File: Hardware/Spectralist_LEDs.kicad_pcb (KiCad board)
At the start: 2 copper layers, 26 parts, among them U1 PCA9956B_LED_Driver

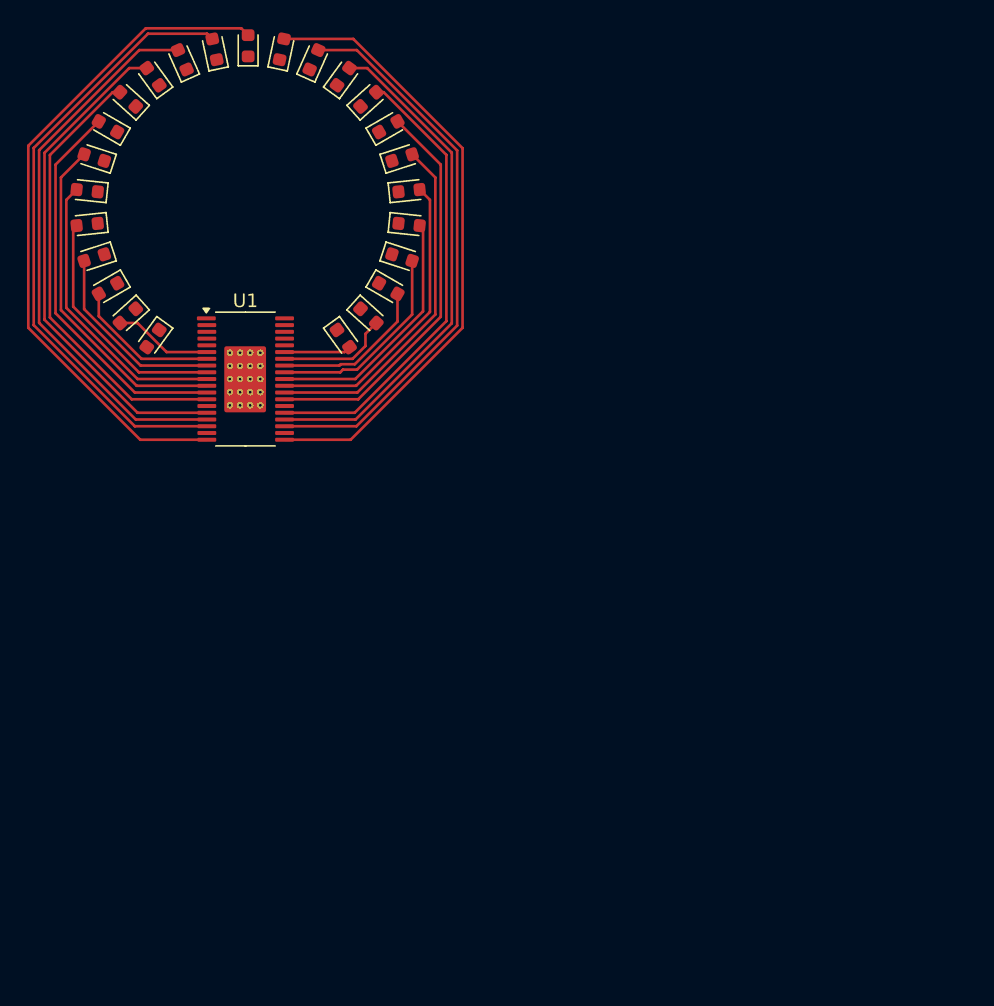
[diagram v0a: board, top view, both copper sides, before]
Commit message: Schematic updates
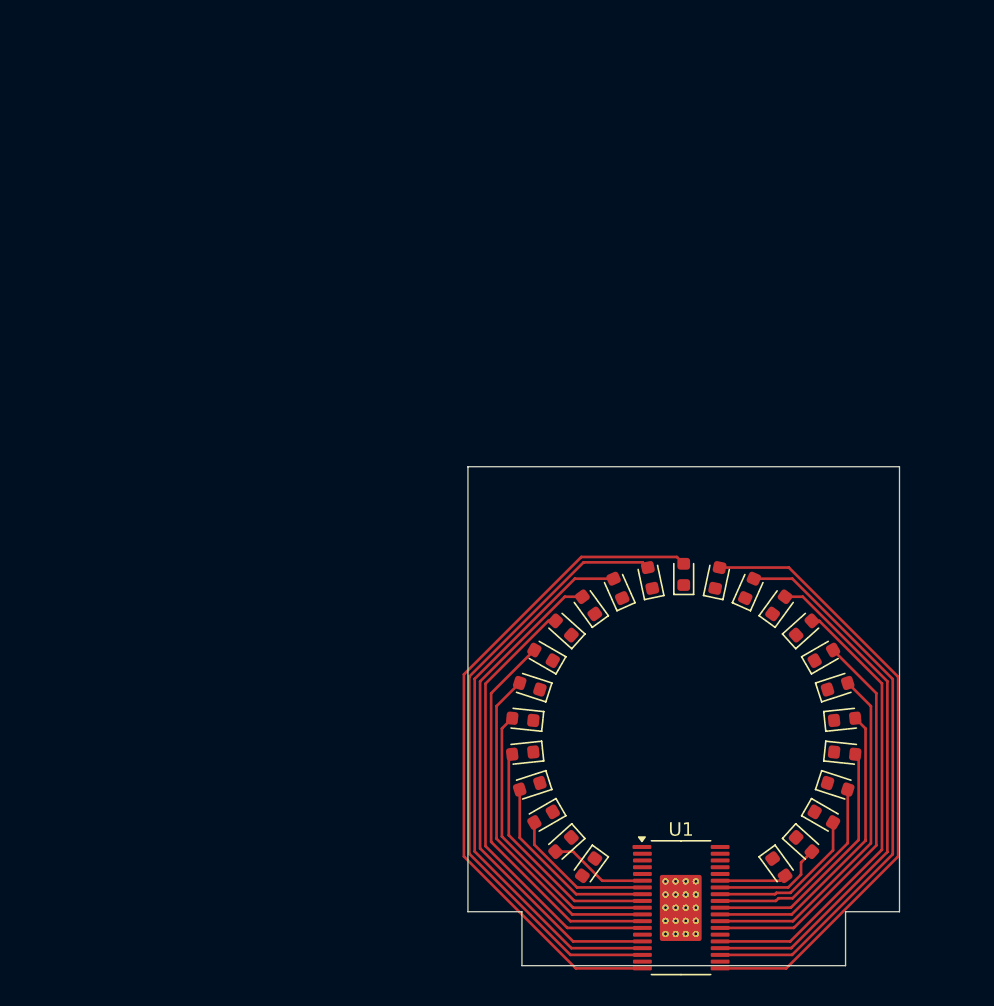
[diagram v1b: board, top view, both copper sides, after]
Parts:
- moved D13 50.8 mm to (132.5, 90.2)
- moved D14 50.8 mm to (134.9, 91.0)
- moved D15 50.8 mm to (137.1, 92.3)
- moved D2 50.8 mm to (119.6, 108.0)
- moved D7 50.8 mm to (119.6, 96.0)
- moved U1 50.8 mm to (129.8, 114.7)
- moved D1 50.8 mm to (121.1, 110.0)
- moved D11 50.8 mm to (127.5, 90.2)
- moved D18 50.8 mm to (141.4, 98.3)
- moved D22 50.8 mm to (140.4, 108.0)
- moved D24 50.8 mm to (137.1, 111.7)
- moved D5 50.8 mm to (118.1, 100.7)
- moved D6 50.8 mm to (118.6, 98.3)
- moved D8 50.8 mm to (121.1, 94.0)
- moved D9 50.8 mm to (122.9, 92.3)
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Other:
- board outline added: 32 x 37 mm

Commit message: Updates to LED board
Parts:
- added C1: 100nF, Capacitor_SMD:C_0603_1608Metric, F.Cu at (135.7, 105.0)
- added C2: 10uF, Capacitor_SMD:C_0805_2012Metric, F.Cu at (112.4, 105.2)
- added J1: Conn_01x03_Pin, Connector_PinHeader_2.54mm:PinHeader_1x03_P2.54mm_Vertical, F.Cu at (132.5, 84.5)
- added J2: Conn_01x02_Pin, Connector_PinHeader_2.54mm:PinHeader_1x02_P2.54mm_Vertical, F.Cu at (112.4, 110.1)
- added J3: Conn_01x02_Pin, Connector_PinHeader_2.54mm:PinHeader_1x02_P2.54mm_Vertical, F.Cu at (147.8, 110.0)
- added R1: 10k, Resistor_SMD:R_0603_1608Metric, F.Cu at (122.4, 105.1)
- added R2: 2k, Resistor_SMD:R_0603_1608Metric, F.Cu at (124.3, 105.1)
- added R3: 10k, Resistor_SMD:R_0603_1608Metric, F.Cu at (138.0, 105.0)
- moved U1 2.61 mm to (129.8, 112.1)
- turned D1 to 42 degrees
- turned D10 to -66 degrees
- turned D11 to -78 degrees
- turned D12 to -90 degrees
- turned D13 to -102 degrees
- turned D14 to -114 degrees
- turned D15 to -126 degrees
- turned D16 to -138 degrees
- turned D17 to -150 degrees
- turned D18 to -162 degrees
- turned D19 to -174 degrees
- turned D2 to 30 degrees
- turned D20 to 174 degrees
- turned D21 to 162 degrees
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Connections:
- D1 pad 1: GND -> Net-(D1-K)
- D1 pad 2: Net-(D1-A) -> +12V
- D10 pad 1: GND -> Net-(D10-K)
- D10 pad 2: Net-(D10-A) -> +12V
- D11 pad 1: GND -> Net-(D11-K)
- D11 pad 2: Net-(D11-A) -> +12V
- D12 pad 1: GND -> Net-(D12-K)
- D12 pad 2: Net-(D12-A) -> +12V
- D13 pad 1: GND -> Net-(D13-K)
- D13 pad 2: Net-(D13-A) -> +12V
- D14 pad 1: GND -> Net-(D14-K)
- D14 pad 2: Net-(D14-A) -> +12V
- D15 pad 1: GND -> Net-(D15-K)
- D15 pad 2: Net-(D15-A) -> +12V
- D16 pad 1: GND -> Net-(D16-K)
- D16 pad 2: Net-(D16-A) -> +12V
- D17 pad 1: GND -> Net-(D17-K)
- D17 pad 2: Net-(D17-A) -> +12V
- D18 pad 1: GND -> Net-(D18-K)
- D18 pad 2: Net-(D18-A) -> +12V
- D19 pad 1: GND -> Net-(D19-K)
- D19 pad 2: Net-(D19-A) -> +12V
- D2 pad 1: GND -> Net-(D2-K)
- D2 pad 2: Net-(D2-A) -> +12V
- D20 pad 1: GND -> Net-(D20-K)
- D20 pad 2: Net-(D20-A) -> +12V
- D21 pad 1: GND -> Net-(D21-K)
- D21 pad 2: Net-(D21-A) -> +12V
- D22 pad 1: GND -> Net-(D22-K)
- D22 pad 2: Net-(D22-A) -> +12V
- D23 pad 1: GND -> Net-(D23-K)
- D23 pad 2: Net-(D23-A) -> +12V
- D24 pad 1: GND -> Net-(D24-K)
- D24 pad 2: Net-(D24-A) -> +12V
- D25 pad 2: unconnected-(D25-A-Pad2) -> Net-(D25-A)
- D3 pad 1: GND -> Net-(D3-K)
- D3 pad 2: Net-(D3-A) -> +12V
- D4 pad 1: GND -> Net-(D4-K)
- D4 pad 2: Net-(D4-A) -> +12V
- D5 pad 1: GND -> Net-(D5-K)
- D5 pad 2: Net-(D5-A) -> +12V
- D6 pad 1: GND -> Net-(D6-K)
- D6 pad 2: Net-(D6-A) -> +12V
- D7 pad 1: GND -> Net-(D7-K)
- D7 pad 2: Net-(D7-A) -> +12V
- D8 pad 1: GND -> Net-(D8-K)
- D8 pad 2: Net-(D8-A) -> +12V
- D9 pad 1: GND -> Net-(D9-K)
- D9 pad 2: Net-(D9-A) -> +12V
- U1 pad 1: unconnected-(U1-REXT-Pad1) -> Net-(U1-REXT)
- U1 pad 10: Net-(D5-A) -> Net-(D5-K)
- U1 pad 11: Net-(D6-A) -> Net-(D6-K)
- U1 pad 12: Net-(D7-A) -> Net-(D7-K)
- U1 pad 13: Net-(D8-A) -> Net-(D8-K)
- U1 pad 15: Net-(D9-A) -> Net-(D9-K)
- U1 pad 16: Net-(D10-A) -> Net-(D10-K)
- U1 pad 17: Net-(D11-A) -> Net-(D11-K)
- U1 pad 19: Net-(D12-A) -> Net-(D12-K)
- U1 pad 20: Net-(D13-A) -> Net-(D13-K)
- U1 pad 22: Net-(D14-A) -> Net-(D14-K)
- U1 pad 23: Net-(D15-A) -> Net-(D15-K)
- U1 pad 24: Net-(D16-A) -> Net-(D16-K)
- U1 pad 26: Net-(D17-A) -> Net-(D17-K)
- U1 pad 27: Net-(D18-A) -> Net-(D18-K)
- U1 pad 28: Net-(D19-A) -> Net-(D19-K)
- U1 pad 29: Net-(D20-A) -> Net-(D20-K)
- U1 pad 30: Net-(D21-A) -> Net-(D21-K)
- U1 pad 31: Net-(D22-A) -> Net-(D22-K)
- U1 pad 32: Net-(D23-A) -> Net-(D23-K)
- U1 pad 33: Net-(D24-A) -> Net-(D24-K)
- U1 pad 35: unconnected-(U1-~{RESET}-Pad35) -> Net-(U1-~{RESET})
- U1 pad 36: unconnected-(U1-SCL-Pad36) -> /LED_SCL
- U1 pad 37: unconnected-(U1-SDA-Pad37) -> /LED_SDA
- U1 pad 38: unconnected-(U1-VDD-Pad38) -> +3.3V
- U1 pad 6: Net-(D1-A) -> Net-(D1-K)
- U1 pad 7: Net-(D2-A) -> Net-(D2-K)
- U1 pad 8: Net-(D3-A) -> Net-(D3-K)
- U1 pad 9: Net-(D4-A) -> Net-(D4-K)
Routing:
- net +12V: track 0.00 -> 73.2 mm, vias 0 -> 1
- net Net-(D12-A): track 50.3 -> 0.00 mm
- net GND: track 0.00 -> 48.4 mm, vias 0 -> 12
- net Net-(D13-A): track 46.6 -> 0.00 mm
- net Net-(D11-A): track 46.0 -> 0.00 mm
- net Net-(D14-A): track 42.3 -> 0.00 mm
- net Net-(D10-A): track 41.6 -> 0.00 mm
- net Net-(D15-K): track 0.00 -> 38.2 mm
- net Net-(D15-A): track 38.2 -> 0.00 mm
- net Net-(D9-K): track 0.00 -> 37.7 mm
- net Net-(D9-A): track 37.5 -> 0.00 mm
- net Net-(D11-K): track 0.00 -> 35.3 mm, vias 0 -> 2
- net Net-(D16-A): track 34.3 -> 0.00 mm
- net Net-(D16-K): track 0.00 -> 34.2 mm
- net Net-(D8-K): track 0.00 -> 33.9 mm
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- added copper zone on B.Cu, net GND
- added copper zone on F.Cu, net GND
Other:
- board size 32 x 37 mm -> 40 x 37 mm

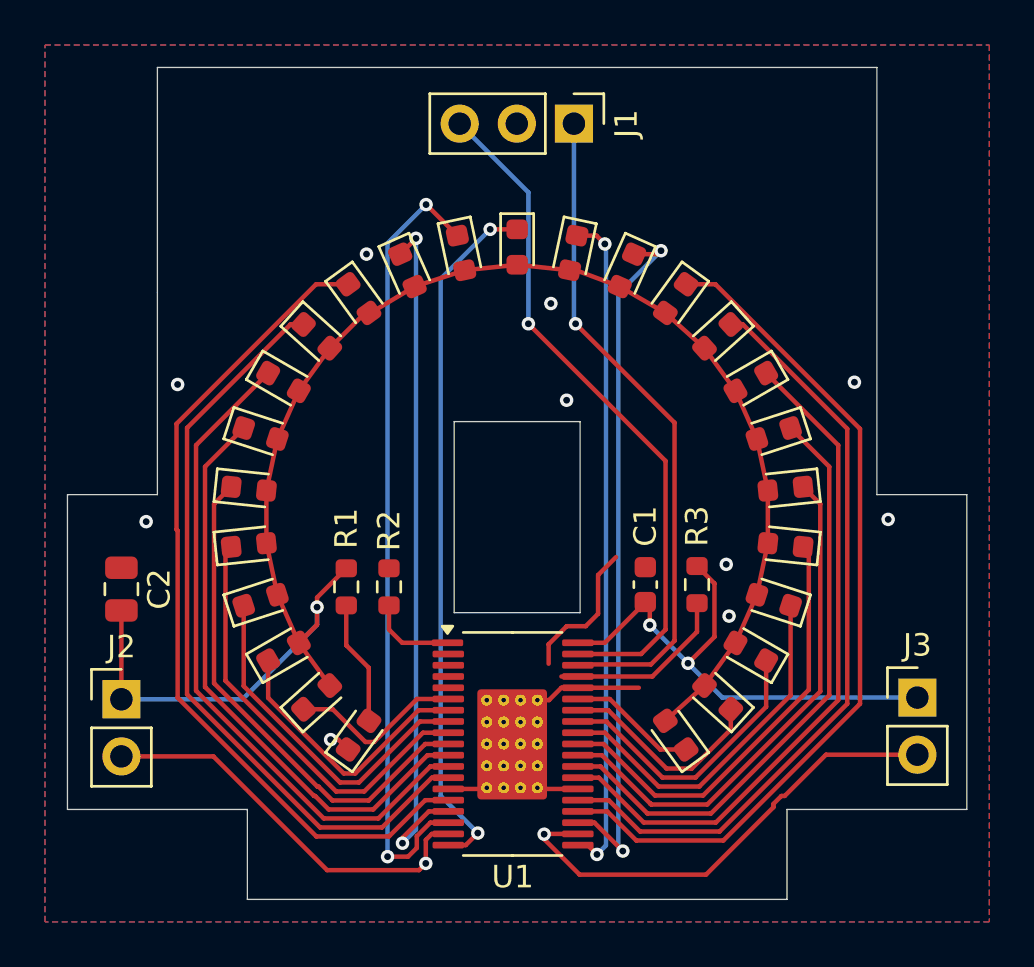
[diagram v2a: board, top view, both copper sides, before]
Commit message: Curvy traces on LED board
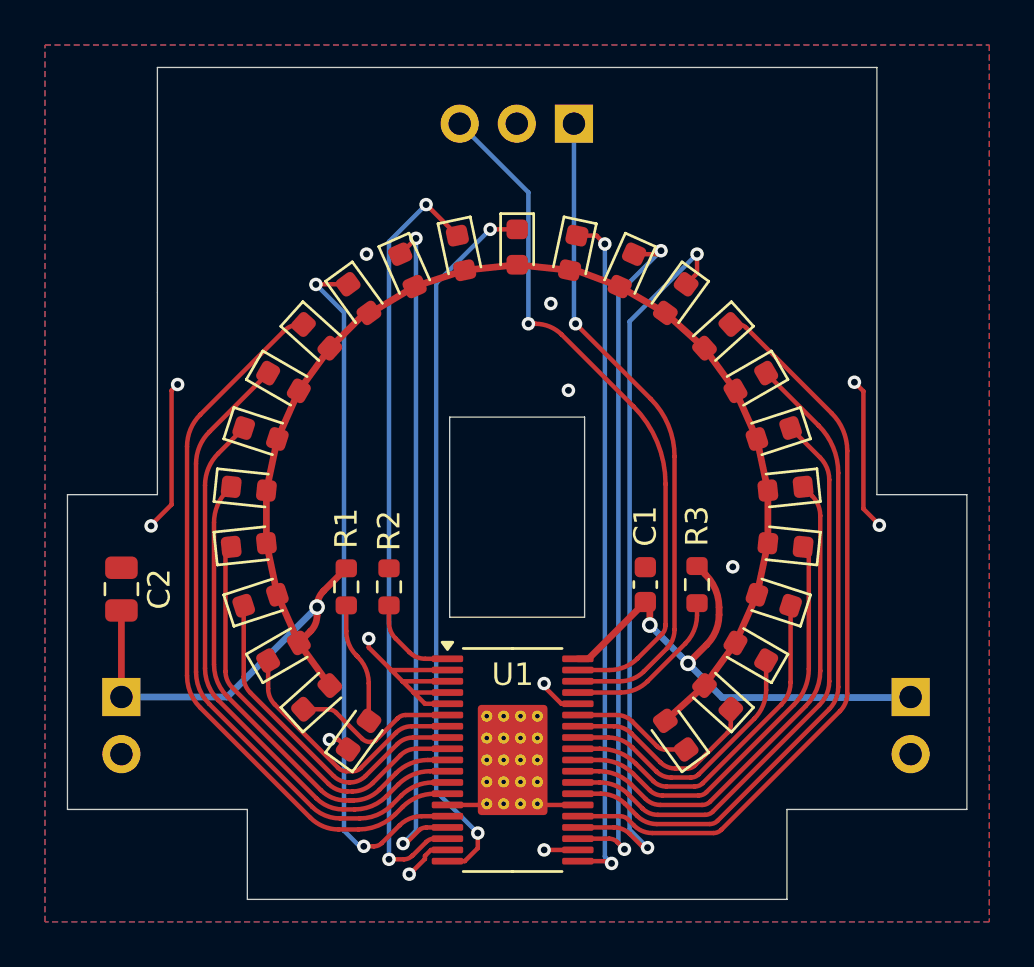
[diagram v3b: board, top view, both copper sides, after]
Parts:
- J1, J2, J3: moved to B.Cu
- moved U1 0.71 mm to (129.8, 112.8)
- moved J3 0.30 mm to (147.5, 110.0), turned to 180 degrees
- moved J2 0.10 mm to (112.4, 110.0), turned to 180 degrees
- turned J1 to 90 degrees
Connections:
- U1 pad 2: unconnected-(U1-AD0-Pad2) -> GND
- U1 pad 3: unconnected-(U1-AD1-Pad3) -> GND
- U1 pad 4: unconnected-(U1-AD2-Pad4) -> GND
- U1 pad 5: unconnected-(U1-~{OE}-Pad5) -> GND
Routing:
- net GND: track 48.4 -> 34.9 mm, vias 12 -> 13
- net Net-(U1-~{RESET}): track 14.6 -> 7.53 mm
- net Net-(D9-K): track 37.7 -> 31.6 mm, vias 0 -> 2
- net Net-(D15-K): track 38.2 -> 32.9 mm, vias 0 -> 2
- net +12V: track 73.2 -> 72.3 mm
- net Net-(D13-K): track 29.8 -> 30.6 mm
- net Net-(D12-K): track 31.2 -> 32.0 mm
- net Net-(D7-K): track 30.0 -> 29.2 mm
- net Net-(D6-K): track 26.3 -> 25.5 mm
- net Net-(D8-K): track 33.9 -> 33.2 mm
- net Net-(D5-K): track 22.7 -> 21.9 mm
- net Net-(D19-K): track 23.2 -> 22.6 mm
- net Net-(D17-K): track 30.5 -> 29.9 mm
- net Net-(D20-K): track 19.6 -> 19.0 mm
- net Net-(D11-K): track 35.3 -> 34.7 mm
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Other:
- outline, holes or cut-outs redrawn

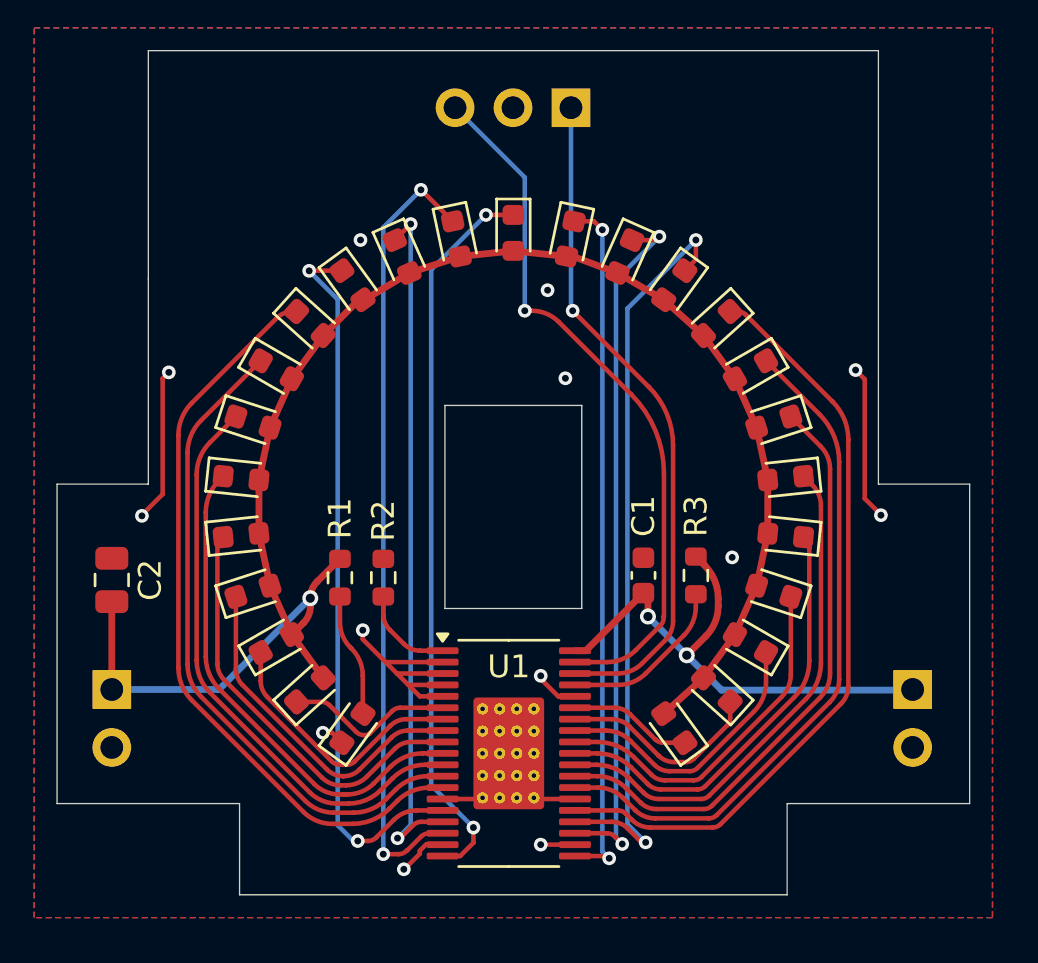
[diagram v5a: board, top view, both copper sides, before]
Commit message: Started adding JLC part numbers
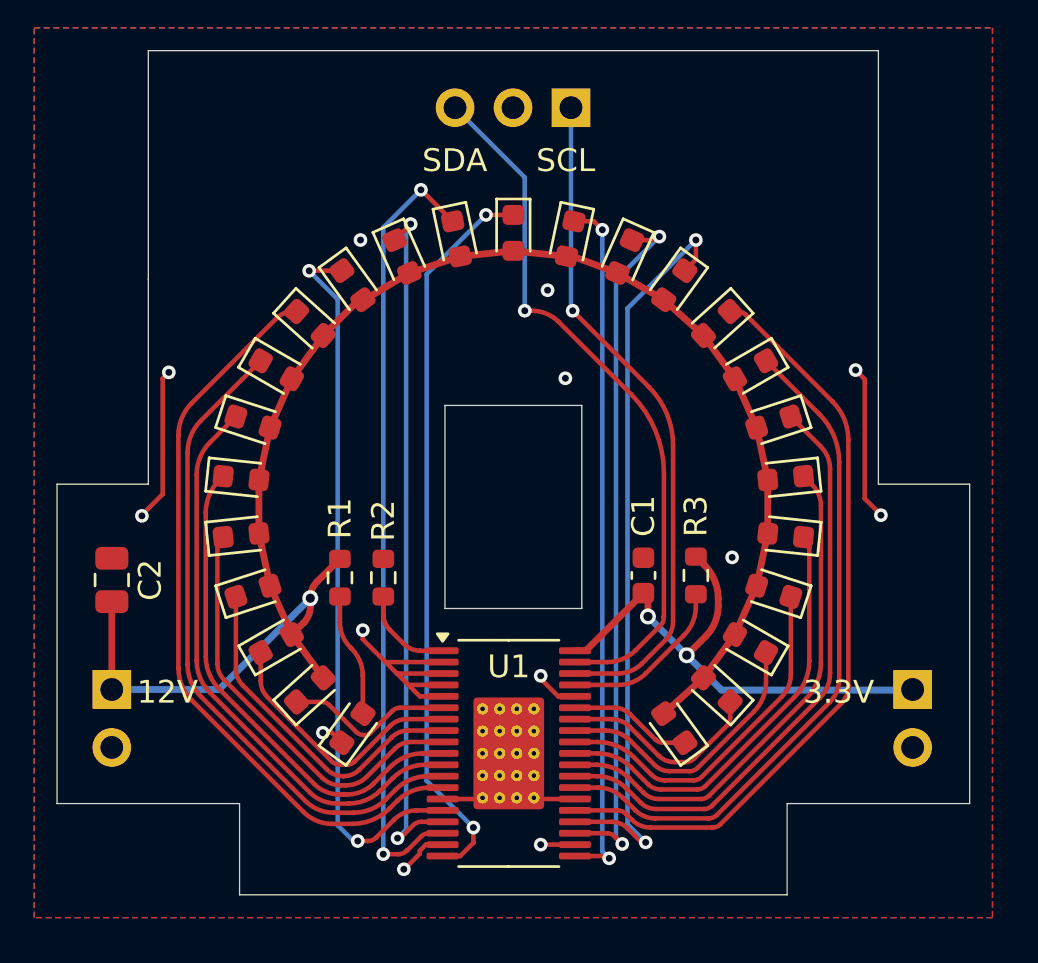
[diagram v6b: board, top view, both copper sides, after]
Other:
- board text added: "12V"
- board text added: "3.3V"
- board text added: "SCL"
- board text added: "SDA"
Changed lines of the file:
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@@
 		(48 "B.Fab" user)
 		(49 "F.Fab" user)
-		(50 "User.1" user)
-		(51 "User.2" user)
-		(52 "User.3" user)
-		(53 "User.4" user)
-		(54 "User.5" user)
-		(55 "User.6" user)
-		(56 "User.7" user)
-		(57 "User.8" user)
-		(58 "User.9" user)
 	)
 	(setup
@@
 			(at 0 2.33 0)
 			(layer "B.SilkS")
+			(hide yes)
 			(effects
 				(font
@@
 			(at 0 2.33 0)
 			(layer "B.SilkS")
+			(hide yes)
 			(effects
 				(font
@@
 			(at 0 2.33 90)
 			(layer "B.SilkS")
+			(hide yes)
 			(effects
 				(font
@@
 		)
 	)
-	(gr_circle
-		(center 58.8 59.1)
-		(end 58.8 76.1)
-		(stroke
-			(width 2)
-			(type default)
-		)
-		(fill none)
-		(layer "F.Mask")
-	)
-	(gr_circle
-		(center 60.9 65)
-		(end 60.9 53.7)
+	(gr_arc
+		(start 123.84 112.265)
+		(mid 130.033685 89.974457)
+		(end 136.1 112.3)
 		(stroke
-			(width 0.1)
+			(width 2.8)
 			(type default)
 		)
-		(fill none)
-		(layer "Dwgs.User")
-	)
-	(gr_circle
-		(center 130 102)
-		(end 142 102)
-		(stroke
-			(width 2)
-			(type default)
-		)
-		(fill none)
 		(layer "Dwgs.User")
 	)
@@
 		(layer "Edge.Cuts")
 	)
+	(gr_circle
+		(center 130 102)
+		(end 142 102)
+		(stroke
+			(width 2)
+			(type default)
+		)
+		(fill none)
+		(layer "F.Fab")
+	)
+	(gr_text "SDA"
+		(at 126 87.4 0)
+		(layer "F.SilkS")
+		(effects
+			(font
+				(size 1 1)
+				(thickness 0.1)
+			)
+			(justify left bottom)
+		)
+	)
+	(gr_text "3.3V"
+		(at 142.7 110.7 0)
+		(layer "F.SilkS")
+		(effects
+			(font
+				(size 1 1)
+				(thickness 0.1)
+			)
+			(justify left bottom)
+		)
+	)
+	(gr_text "12V"
+		(at 113.5 110.7 0)
+		(layer "F.SilkS")
+		(effects
+			(font
+				(size 1 1)
+				(thickness 0.1)
+			)
+			(justify left bottom)
+		)
+	)
+	(gr_text "SCL"
+		(at 131 87.4 0)
+		(layer "F.SilkS")
+		(effects
+			(font
+				(size 1 1)
+				(thickness 0.1)
+			)
+			(justify left bottom)
+		)
+	)
 	(segment
 		(start 125.22038 117.87962)
@@
 	)
 	(segment
+		(start 125.3 116.140915)
+		(end 124.923586 116.517329)
+		(width 0.2)
+		(layer "B.Cu")
+		(net 12)
+	)
+	(segment
 		(start 125.5 89.599996)
-		(end 125.5 115.940915)
+		(end 125.3 89.799996)
 		(width 0.2)
 		(layer "B.Cu")
@@
 	)
 	(segment
-		(start 125.5 115.940915)
-		(end 124.923586 116.517329)
+		(start 125.3 89.799996)
+		(end 125.3 116.140915)
 		(width 0.2)
 		(layer "B.Cu")
@@
 	)
 	(segment
-		(start 128.25 116.05)
-		(end 126.4 114.2)
+		(start 126.2 91.799998)
+		(end 128.8 89.199998)
 		(width 0.2)
 		(layer "B.Cu")
@@
 	)
 	(segment
-		(start 126.4 114.2)
-		(end 126.4 91.599998)
+		(start 128.25 116.05)
+		(end 126.2 114)
 		(width 0.2)
 		(layer "B.Cu")
@@
 	)
 	(segment
-		(start 126.4 91.599998)
-		(end 128.8 89.199998)
+		(start 126.2 114)
+		(end 126.2 91.799998)
 		(width 0.2)
 		(layer "B.Cu")
